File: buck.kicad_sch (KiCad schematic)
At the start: 35 parts, among them J6 Conn_01x02_Socket, Q10 BSC059N04LS6, Q9 BSC059N04LS6, U6 BQ24640

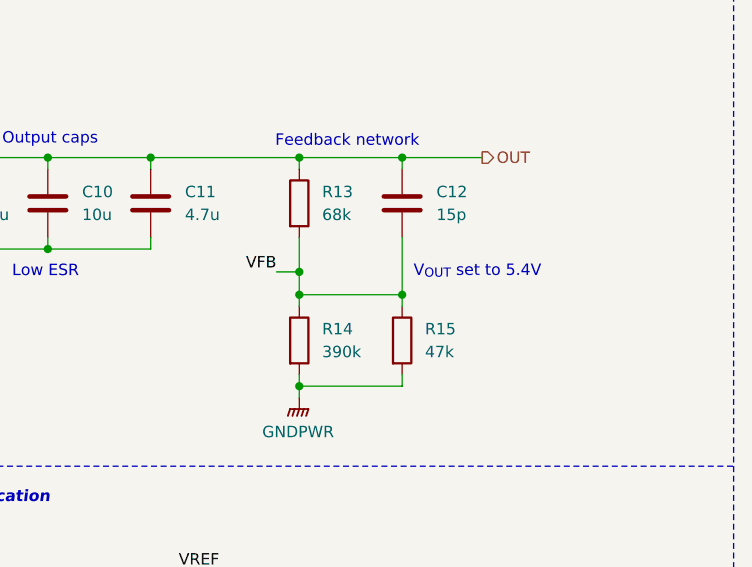
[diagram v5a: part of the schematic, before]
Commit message: Updating buck converter to work with new 2S2P supercap stackup
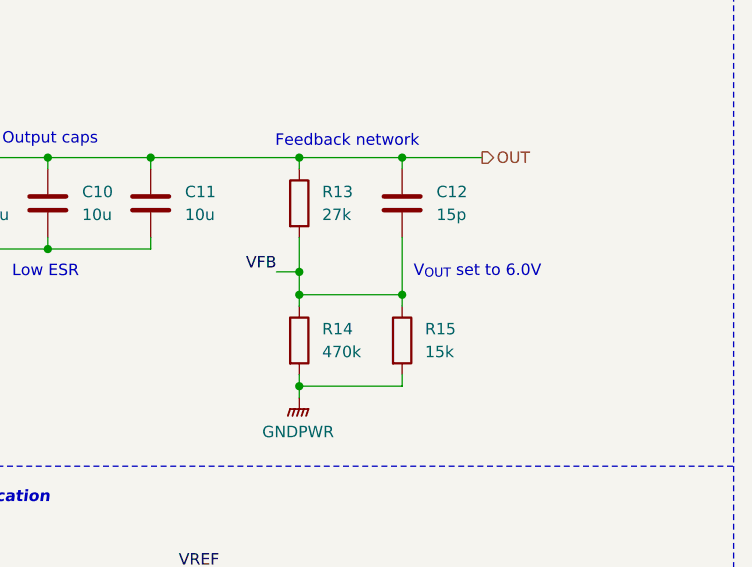
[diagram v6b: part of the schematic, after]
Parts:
- C11: value 4.7u -> 10u
- R13: value 68k -> 27k
- R14: value 390k -> 470k
- R15: value 47k -> 15k
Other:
- note added: "V_{OUT} set to 6.0V"
- note removed: "V_{OUT} set to 5.4V"
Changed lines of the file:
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@@
 		)
 	)
-	(text "V_{OUT} set to 5.4V"
+	(text "V_{OUT} set to 6.0V"
 		(exclude_from_sim no)
 		(at 245.11 82.55 0)
@@
 			)
 		)
-		(property "Value" "68k"
+		(property "Value" "27k"
 			(at 234.95 76.1999 0)
 			(effects
@@
 			)
 		)
-		(property "Datasheet" "https://www.mouser.com/datasheet/2/196/Infineon_BSC015NE2LS5I_DataSheet_v02_01_EN-3360635.pdf"
+		(property "Datasheet" "https://www.mouser.com/datasheet/2/196/Infineon_BSC059N04LS6_DataSheet_v02_01_EN-3360636.pdf"
 			(at 146.05 59.69 0)
 			(effects
@@
 	)
 	(symbol
-		(lib_id "Device:C")
-		(at 215.9 74.93 0)
+		(lib_id "power:GNDPWR")
+		(at 226.06 143.51 0)
 		(unit 1)
 		(exclude_from_sim no)
@@
 		(dnp no)
 		(fields_autoplaced yes)
-		(property "Reference" "C11"
-			(at 219.71 73.6599 0)
+		(property "Reference" "#PWR038"
+			(at 226.06 148.59 0)
 			(effects
 				(font
 					(size 1.27 1.27)
 				)
-				(justify left)
+				(hide yes)
 			)
 		)
-		(property "Value" "4.7u"
-			(at 219.71 76.1999 0)
+		(property "Value" "GNDPWR"
+			(at 225.933 147.32 0)
 			(effects
 				(font
 					(size 1.27 1.27)
 				)
-				(justify left)
 			)
 		)
-		(property "Footprint" "Capacitor_SMD:C_0805_2012Metric_Pad1.18x1.45mm_HandSolder"
-			(at 216.8652 78.74 0)
+		(property "Footprint" ""
+			(at 226.06 144.78 0)
 			(effects
 				(font
@@
 			)
 		)
-		(property "Datasheet" "https://www.mouser.com/datasheet/2/585/MLCC-1837944.pdf"
-			(at 215.9 74.93 0)
+		(property "Datasheet" ""
+			(at 226.06 144.78 0)
 			(effects
 				(font
@@
 			)
 		)
-		(property "Description" "Unpolarized capacitor"
-			(at 215.9 74.93 0)
+		(property "Description" "Power symbol creates a global label with name \"GNDPWR\" , global ground"
+			(at 226.06 143.51 0)
 			(effects
 				(font
@@
 			)
 		)
-		(property "Mouser Part Number" "187-CL21A106KAYNNNE"
-			(at 215.9 74.93 0)
-			(effects
-				(font
-					(size 1.27 1.27)
+		(pin "1"
+		)
+		(instances
+			(project "Input Buck Rev1"
+				(path "/3b860e9b-bc45-416d-b09e-893d0b22ad61/013921e8-055b-4930-a2c6-9be4a4ca23d3"
+					(reference "#PWR0105")
+					(unit 1)
+				)
+			)
+			(project "SupercapManager"
+				(path "/6197145b-e7d4-44cc-9d90-537b6501bf60/388608c4-ca49-4b14-9684-8f150e280879"
+					(reference "#PWR038")
+					(unit 1)
 				)
-				(hide yes)
 			)
 		)
-		(property "Height" ""
-			(at 215.9 74.93 0)
+	)
+	(symbol
+		(lib_id "Device:R")
+		(at 124.46 59.69 90)
+		(unit 1)
+		(exclude_from_sim no)
+		(in_bom yes)
+		(on_board yes)
+		(dnp no)
+		(property "Reference" "R32"
+			(at 121.412 59.182 90)
 			(effects
 				(font
 					(size 1.27 1.27)
 				)
+				(justify left top)
 			)
 		)
-		(property "Manufacturer_Name" ""
-			(at 215.9 74.93 0)
+		(property "Value" "0"
+			(at 127.508 59.182 90)
 			(effects
 				(font
 					(size 1.27 1.27)
 				)
+				(justify right top)
 			)
 		)
-		(property "Manufacturer_Part_Number" ""
-			(at 215.9 74.93 0)
+		(property "Footprint" "Resistor_SMD:R_0603_1608Metric_Pad0.98x0.95mm_HandSolder"
+			(at 124.46 61.468 90)
 			(effects
 				(font
 					(size 1.27 1.27)
 				)
+				(hide yes)
 			)
 		)
-		(property "Mouser Price/Stock" ""
-			(at 215.9 74.93 0)
+		(property "Datasheet" "~"
+			(at 124.46 59.69 0)
 			(effects
 				(font
 					(size 1.27 1.27)
 				)
+				(hide yes)
 			)
 		)
-		(pin "1"
-		)
-		(pin "2"
-		)
-		(instances
-			(project "SupercapManager"
-				(path "/6197145b-e7d4-44cc-9d90-537b6501bf60/388608c4-ca49-4b14-9684-8f150e280879"
-					(reference "C11")
-					(unit 1)
-				)
-			)
-		)
-	)
-	(symbol
-		(lib_id "power:GNDPWR")
-		(at 226.06 143.51 0)
-		(unit 1)
-		(exclude_from_sim no)
-		(in_bom yes)
-		(on_board yes)
-		(dnp no)
-		(fields_autoplaced yes)
-		(property "Reference" "#PWR038"
-			(at 226.06 148.59 0)
+		(property "Description" "Resistor"
+			(at 124.46 59.69 0)
 			(effects
 				(font
@@
 			)
 		)
-		(property "Value" "GNDPWR"
-			(at 225.933 147.32 0)
+		(property "Height" ""
+			(at 124.46 59.69 0)
 			(effects
 				(font
@@
 			)
 		)
-		(property "Footprint" ""
-			(at 226.06 144.78 0)
+		(property "Manufacturer_Name" ""
+			(at 124.46 59.69 0)
 			(effects
 				(font
 					(size 1.27 1.27)
 				)
-				(hide yes)
 			)
 		)
-		(property "Datasheet" ""
-			(at 226.06 144.78 0)
+		(property "Manufacturer_Part_Number" ""
+			(at 124.46 59.69 0)
 			(effects
 				(font
 					(size 1.27 1.27)
 				)
-				(hide yes)
 			)
 		)
-		(property "Description" "Power symbol creates a global label with name \"GNDPWR\" , global ground"
-			(at 226.06 143.51 0)
+		(property "Mouser Price/Stock" ""
+			(at 124.46 59.69 0)
 			(effects
 				(font
 					(size 1.27 1.27)
 				)
-				(hide yes)
 			)
 		)
+		(pin "2"
+		)
 		(pin "1"
 		)
 		(instances
-			(project "Input Buck Rev1"
-				(path "/3b860e9b-bc45-416d-b09e-893d0b22ad61/013921e8-055b-4930-a2c6-9be4a4ca23d3"
-					(reference "#PWR0105")
-					(unit 1)
-				)
-			)
 			(project "SupercapManager"
 				(path "/6197145b-e7d4-44cc-9d90-537b6501bf60/388608c4-ca49-4b14-9684-8f150e280879"
-					(reference "#PWR038")
+					(reference "R32")
 					(unit 1)
 				)
@@
 	)
 	(symbol
-		(lib_id "Device:R")
-		(at 124.46 59.69 90)
+		(lib_id "Device:C")
+		(at 215.9 74.93 0)
 		(unit 1)
 		(exclude_from_sim no)
@@
 		(on_board yes)
 		(dnp no)
-		(property "Reference" "R32"
-			(at 121.412 59.182 90)
+		(fields_autoplaced yes)
+		(property "Reference" "C11"
+			(at 219.71 73.6599 0)
 			(effects
 				(font
 					(size 1.27 1.27)
 				)
-				(justify left top)
+				(justify left)
 			)
 		)
-		(property "Value" "0"
-			(at 127.508 59.182 90)
+		(property "Value" "10u"
+			(at 219.71 76.1999 0)
 			(effects
 				(font
 					(size 1.27 1.27)
 				)
-				(justify right top)
+				(justify left)
 			)
 		)
-		(property "Footprint" "Resistor_SMD:R_0603_1608Metric_Pad0.98x0.95mm_HandSolder"
-			(at 124.46 61.468 90)
+		(property "Footprint" "Capacitor_SMD:C_0805_2012Metric_Pad1.18x1.45mm_HandSolder"
+			(at 216.8652 78.74 0)
 			(effects
 				(font
@@
 			)
 		)
-		(property "Datasheet" "~"
-			(at 124.46 59.69 0)
+		(property "Datasheet" "https://www.mouser.com/datasheet/2/585/MLCC-1837944.pdf"
+			(at 215.9 74.93 0)
 			(effects
 				(font
@@
 			)
 		)
-		(property "Description" "Resistor"
-			(at 124.46 59.69 0)
+		(property "Description" "Unpolarized capacitor"
+			(at 215.9 74.93 0)
+			(effects
+				(font
+					(size 1.27 1.27)
+				)
+				(hide yes)
+			)
+		)
+		(property "Mouser Part Number" "187-CL21A106KAYNNNE"
+			(at 215.9 74.93 0)
 			(effects
 				(font
@@
 		)
 		(property "Height" ""
-			(at 124.46 59.69 0)
+			(at 215.9 74.93 0)
 			(effects
 				(font
@@
 		)
 		(property "Manufacturer_Name" ""
-			(at 124.46 59.69 0)
+			(at 215.9 74.93 0)
 			(effects
 				(font
@@
 		)
 		(property "Manufacturer_Part_Number" ""
-			(at 124.46 59.69 0)
+			(at 215.9 74.93 0)
 			(effects
 				(font
@@
 		)
 		(property "Mouser Price/Stock" ""
-			(at 124.46 59.69 0)
+			(at 215.9 74.93 0)
 			(effects
 				(font
@@
 			)
 		)
-		(pin "2"
-		)
 		(pin "1"
 		)
+		(pin "2"
+		)
 		(instances
 			(project "SupercapManager"
 				(path "/6197145b-e7d4-44cc-9d90-537b6501bf60/388608c4-ca49-4b14-9684-8f150e280879"
-					(reference "R32")
+					(reference "C11")
 					(unit 1)
 				)
@@
 			)
 		)
-		(property "Value" "47k"
+		(property "Value" "15k"
 			(at 246.38 91.4399 0)
 			(effects
@@
 			)
 		)
-		(property "Datasheet" "https://www.mouser.com/datasheet/2/196/Infineon_BSC015NE2LS5I_DataSheet_v02_01_EN-3360635.pdf"
+		(property "Datasheet" "https://www.mouser.com/datasheet/2/196/Infineon_BSC059N04LS6_DataSheet_v02_01_EN-3360636.pdf"
 			(at 146.05 76.2 0)
 			(effects
@@
 			)
 		)
-		(property "Value" "390k"
+		(property "Value" "470k"
 			(at 234.95 91.4399 0)
 			(effects

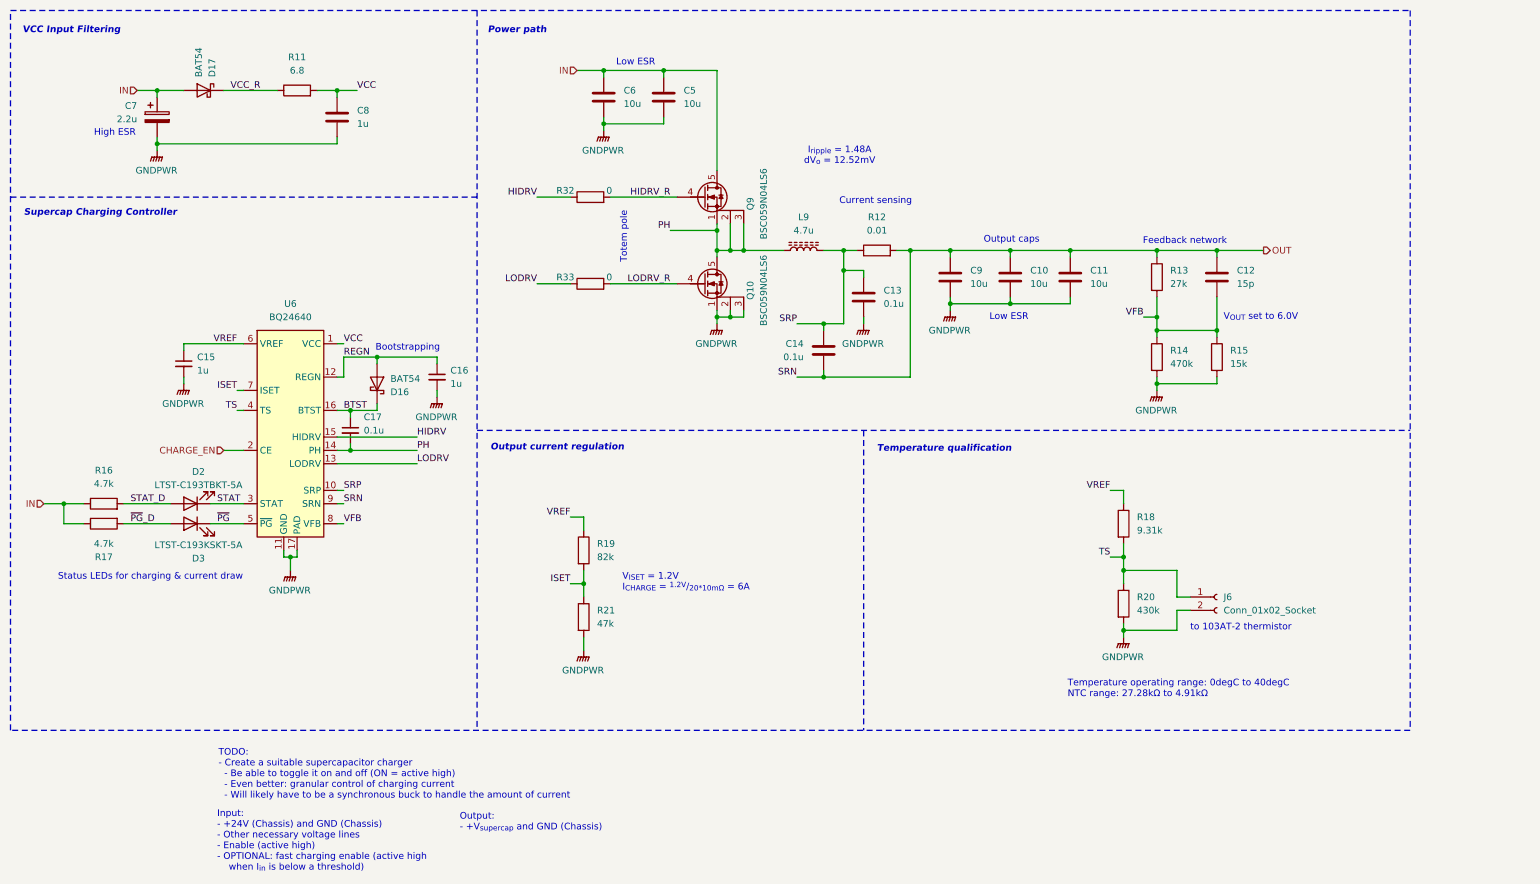
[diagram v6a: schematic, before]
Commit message: Reannotate schematic
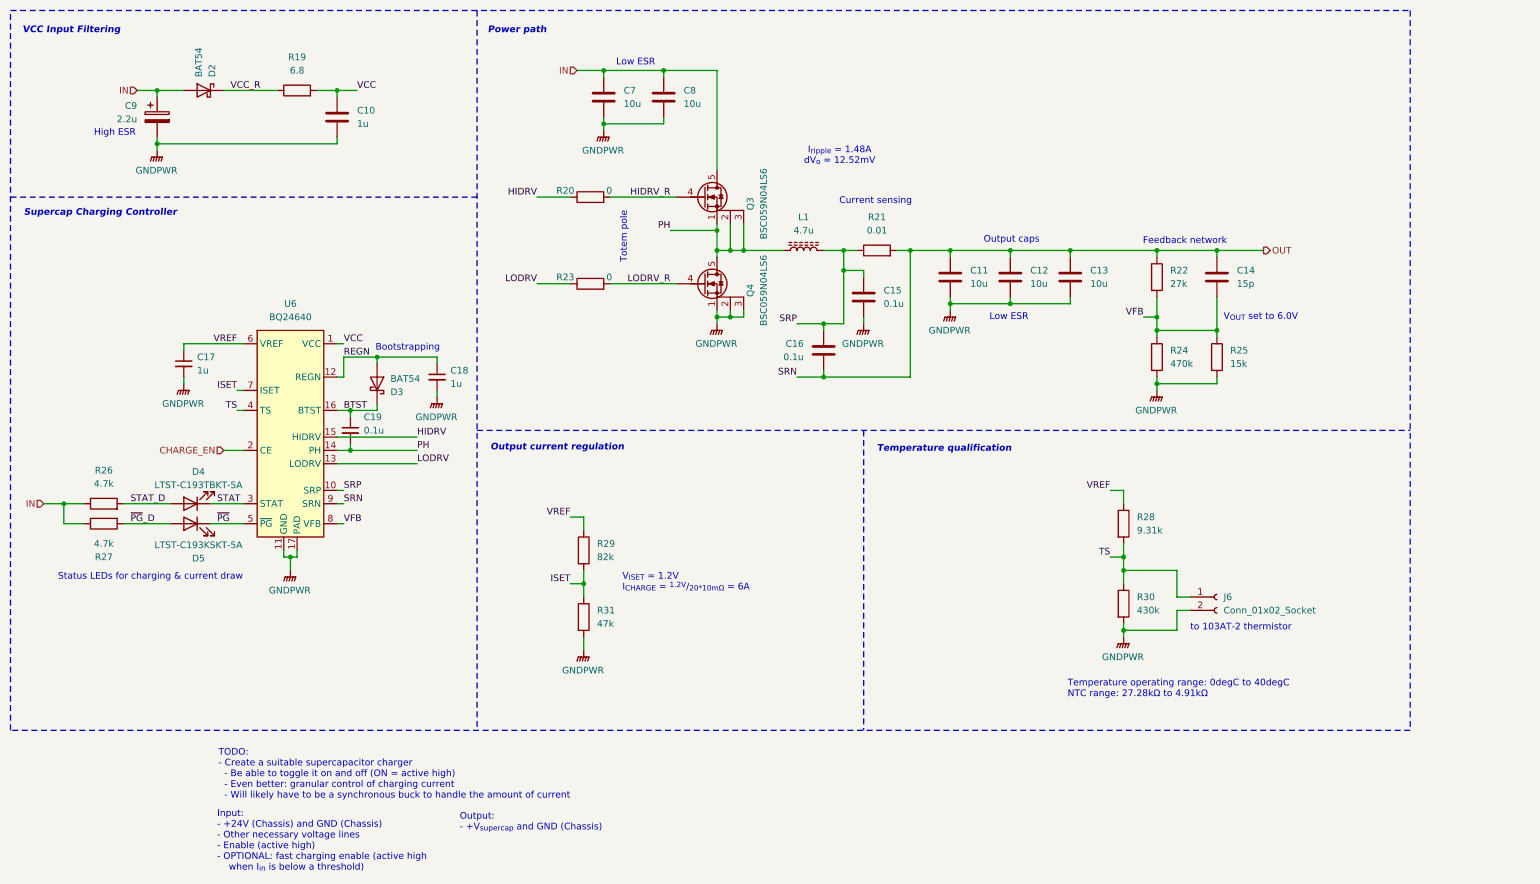
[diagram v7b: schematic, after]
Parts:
- renumbered C8 to C10, C9 to C11, C10 to C12, C11 to C13, C12 to C14, C13 to C15, C14 to C16, C15 to C17, C16 to C18, C17 to C19, C6 to C7, C5 to C8, C7 to C9, D17 to D2, D16 to D3, D2 to D4, D3 to D5, L9 to L1, Q9 to Q3, Q10 to Q4, R11 to R19, R32 to R20, R12 to R21, R13 to R22, R33 to R23, R14 to R24, R15 to R25, R16 to R26, R17 to R27, R18 to R28, R19 to R29, R20 to R30, R21 to R31

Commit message: Adjusted some things + changed discharge to have a smaller time constant
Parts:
- C14: Mouser Part Number (none) -> 791-0603N150F500CT
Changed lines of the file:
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@@
 			)
 		)
-		(property "Datasheet" "~"
+		(property "Datasheet" "https://www.mouser.com/datasheet/2/447/KEM_C1006_X5R_SMD-3316465.pdf"
 			(at 95.25 93.98 0)
 			(effects
@@
 			)
 		)
-		(property "Datasheet" "~"
+		(property "Datasheet" "https://www.mouser.com/datasheet/2/447/KEM_C1006_X5R_SMD-3316465.pdf"
 			(at 46.99 91.44 0)
 			(effects
@@
 			)
 		)
-		(property "Datasheet" "~"
+		(property "Datasheet" "https://www.mouser.com/datasheet/2/210/WTC_MLCC_General_Purpose-1534899.pdf"
 			(at 243.84 74.93 0)
 			(effects
@@
 			)
 		)
+		(property "Mouser Part Number" "791-0603N150F500CT"
+			(at 243.84 74.93 0)
+			(effects
+				(font
+					(size 1.27 1.27)
+				)
+				(hide yes)
+			)
+		)
 		(pin "1"
 		)
@@
 			)
 		)
-		(property "Datasheet" "~"
+		(property "Datasheet" "https://www.mouser.com/datasheet/2/447/KEM_C1006_X5R_SMD-3316465.pdf"
 			(at 76.2 44.45 0)
 			(effects
